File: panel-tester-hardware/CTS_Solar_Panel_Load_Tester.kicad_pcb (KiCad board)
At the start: 2 copper layers, 102 x 64.5 mm, 13 parts, among them J1 Screw_Terminal_01x02, J2 Conn_01x02_Pin, J3 Conn_01x07, J4 Conn_01x20_Pin, J5 Conn_01x20_Pin, Q2 2N7002, U1 INA219AxD, U3 LM311

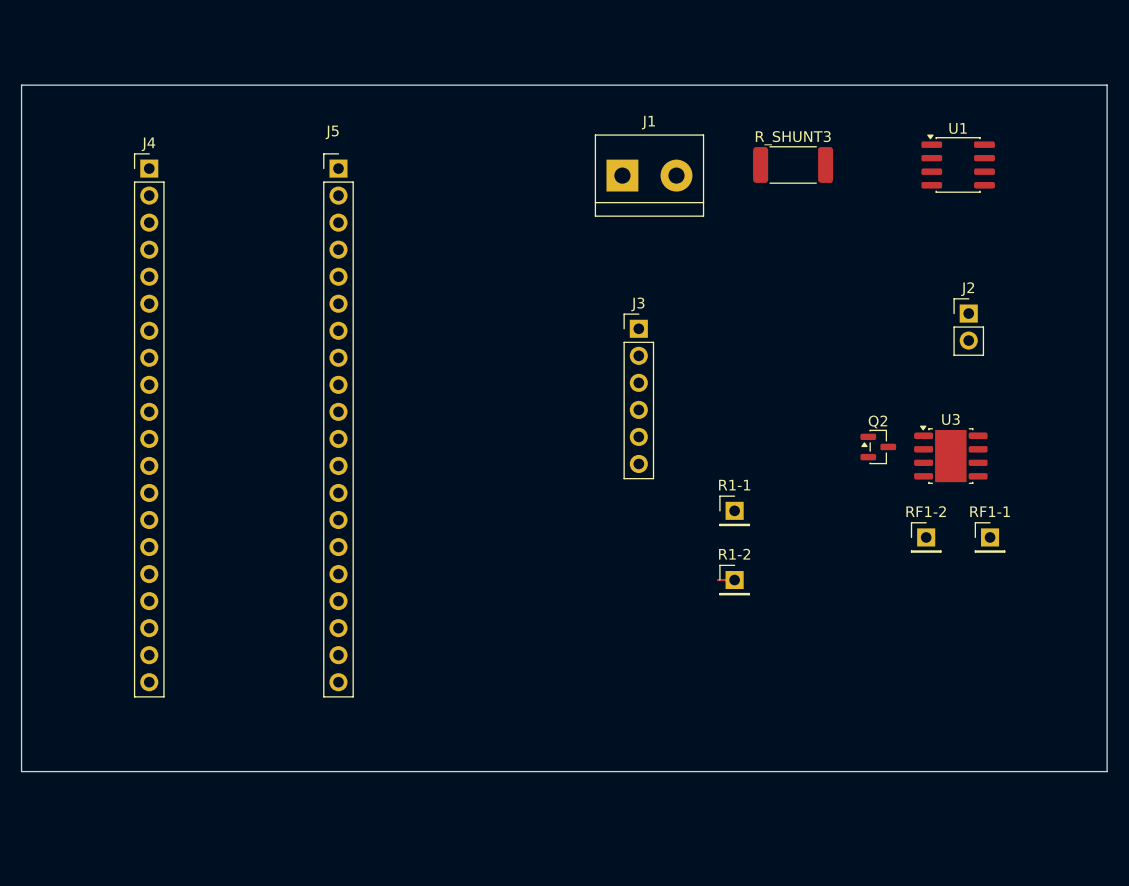
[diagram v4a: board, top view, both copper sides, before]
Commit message: PCB passes DRC
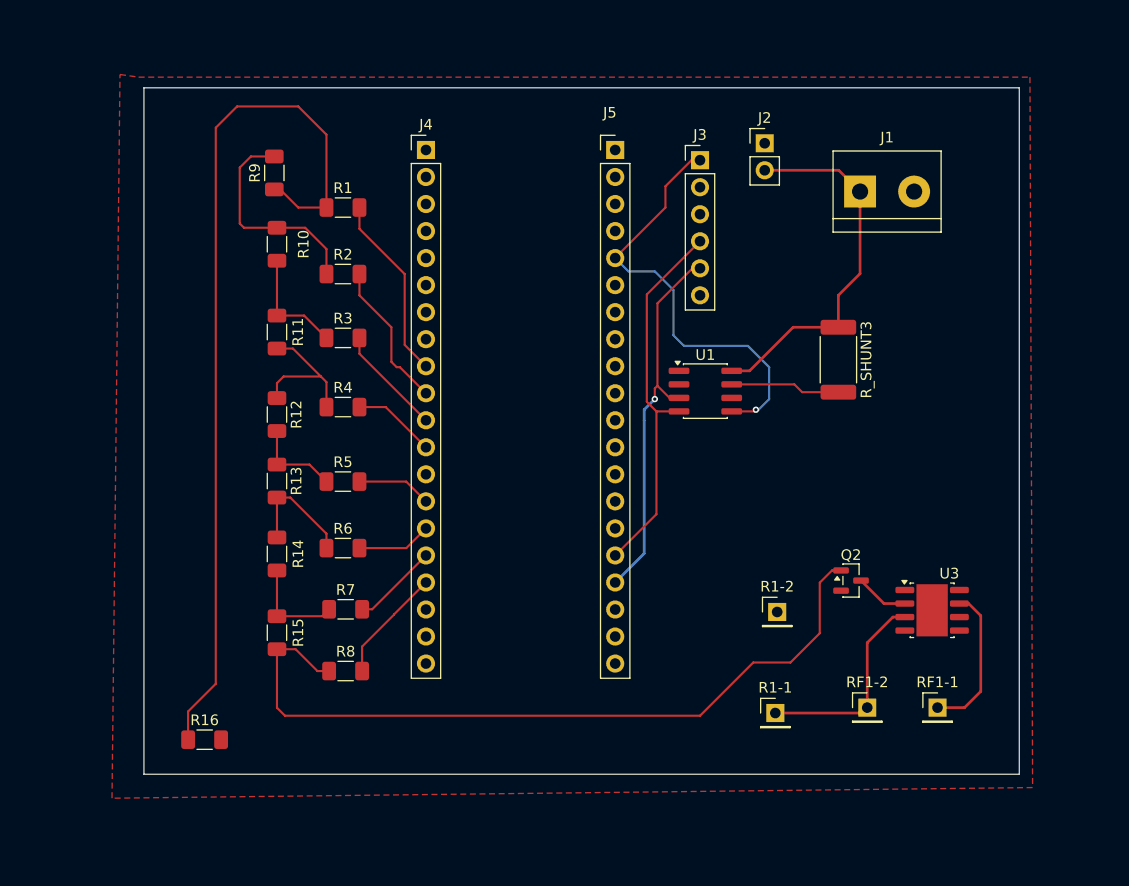
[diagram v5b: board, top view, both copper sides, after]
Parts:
- added R1: 2k, Resistor_SMD:R_1206_3216Metric_Pad1.30x1.75mm_HandSolder, F.Cu at (108.2, 65.0)
- added R10: 1k, Resistor_SMD:R_1206_3216Metric_Pad1.30x1.75mm_HandSolder, F.Cu at (102.0, 68.5)
- added R11: 1k, Resistor_SMD:R_1206_3216Metric_Pad1.30x1.75mm_HandSolder, F.Cu at (102.0, 76.7)
- added R12: 1k, Resistor_SMD:R_1206_3216Metric_Pad1.30x1.75mm_HandSolder, F.Cu at (102.0, 84.5)
- added R13: 1k, Resistor_SMD:R_1206_3216Metric_Pad1.30x1.75mm_HandSolder, F.Cu at (102.0, 90.7)
- added R14: 1k, Resistor_SMD:R_1206_3216Metric_Pad1.30x1.75mm_HandSolder, F.Cu at (102.0, 97.5)
- added R15: 1k, Resistor_SMD:R_1206_3216Metric_Pad1.30x1.75mm_HandSolder, F.Cu at (102.0, 105.0)
- added R16: 2k, Resistor_SMD:R_1206_3216Metric_Pad1.30x1.75mm_HandSolder, F.Cu at (95.2, 115.0)
- added R2: 2k, Resistor_SMD:R_1206_3216Metric_Pad1.30x1.75mm_HandSolder, F.Cu at (108.2, 71.2)
- added R3: 2k, Resistor_SMD:R_1206_3216Metric_Pad1.30x1.75mm_HandSolder, F.Cu at (108.2, 77.2)
- added R4: 2k, Resistor_SMD:R_1206_3216Metric_Pad1.30x1.75mm_HandSolder, F.Cu at (108.2, 83.8)
- added R5: 2k, Resistor_SMD:R_1206_3216Metric_Pad1.30x1.75mm_HandSolder, F.Cu at (108.2, 90.8)
- added R6: 2k, Resistor_SMD:R_1206_3216Metric_Pad1.30x1.75mm_HandSolder, F.Cu at (108.2, 97.0)
- added R7: 2k, Resistor_SMD:R_1206_3216Metric_Pad1.30x1.75mm_HandSolder, F.Cu at (108.5, 102.8)
- added R8: 2k, Resistor_SMD:R_1206_3216Metric_Pad1.30x1.75mm_HandSolder, F.Cu at (108.5, 108.6)
- added R9: 1k, Resistor_SMD:R_1206_3216Metric_Pad1.30x1.75mm_HandSolder, F.Cu at (101.8, 61.8)
- moved U1 31.9 mm to (142.2, 82.2)
- moved J4 26.1 mm to (116.0, 59.6)
- moved J5 26.1 mm to (133.8, 59.6)
- moved J2 25.0 mm to (147.8, 59.0)
- moved J1 22.4 mm to (156.8, 63.5)
- moved R1-1 19.4 mm to (148.8, 112.5)
- moved R_SHUNT3 18.8 mm to (154.8, 79.3), turned to -90 degrees
- moved RF1-2 16.9 mm to (157.5, 112.0)
- moved J3 16.9 mm to (141.8, 60.5)
- moved RF1-1 16.7 mm to (164.1, 112.0)
- moved U3 14.6 mm to (163.6, 102.8)
- moved Q2 12.8 mm to (155.9, 100.0)
- moved R1-2 5.00 mm to (149.0, 103.0)
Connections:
- J4 pad 10: unconnected-(J4-Pin_10-Pad10) -> GP7
- J4 pad 11: unconnected-(J4-Pin_11-Pad11) -> GP8
- J4 pad 12: unconnected-(J4-Pin_12-Pad12) -> GP9
- J4 pad 14: unconnected-(J4-Pin_14-Pad14) -> GP10
- J4 pad 15: unconnected-(J4-Pin_15-Pad15) -> GP11
- J4 pad 16: unconnected-(J4-Pin_16-Pad16) -> GP12
- J4 pad 17: unconnected-(J4-Pin_17-Pad17) -> GP13_MSB
- J4 pad 9: unconnected-(J4-Pin_9-Pad9) -> GP6_LSB
- J5 pad 16: unconnected-(J5-Pin_16-Pad16) -> MCU_I2C_SCL
- J5 pad 17: unconnected-(J5-Pin_17-Pad17) -> MCU_I2C_SDA
- J5 pad 18: unconnected-(J5-Pin_18-Pad18) -> GND
- J5 pad 5: unconnected-(J5-Pin_5-Pad5) -> +3V3
- Q2 pad 1: unconnected-(Q2-G-Pad1) -> RAMP
- U3 pad 1: Net-(U3-GND) -> GND
- U3 pad 4: Net-(U3-GND) -> GND
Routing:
- net Net-(R1-Pad1): track 0.00 -> 83.4 mm
- net RAMP: track 0.00 -> 73.0 mm
- net +3V3: track 0.00 -> 41.2 mm, vias 0 -> 1
- net MCU_I2C_SDA: track 0.00 -> 35.7 mm, vias 0 -> 1
- net MCU_I2C_SCL: track 0.00 -> 35.7 mm
- net V_SOLAR_INPUT_POS: track 0.00 -> 35.1 mm
- net Net-(R10-Pad1): track 0.00 -> 20.5 mm
- net Net-(R1-1-Pin_1): track 0.00 -> 19.5 mm
- net GP6_LSB: track 0.00 -> 17.5 mm
- net Net-(RF1-1-Pin_1): track 0.00 -> 14.3 mm
- net Net-(R11-Pad2): track 0.00 -> 14.1 mm
- net GP7: track 0.00 -> 14.0 mm
- net Net-(R13-Pad2): track 0.00 -> 11.2 mm
- net GP13_MSB: track 0.00 -> 10.8 mm
- net Net-(R10-Pad2): track 0.00 -> 10.7 mm
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- added copper zone on F.Cu, net GND
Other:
- board size 102 x 64.5 mm -> 82.2 x 64.5 mm

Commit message: checklist almost done
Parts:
- added G***: LOGO, 00-logo-footprint-library:ctslogo1x2cm, F.Cu at (147.2, 92.8)
- moved R16 56.8 mm to (108.2, 59.8)
- moved J1 7.96 mm to (154.2, 71.0), turned to 90 degrees
- moved Q2 4.36 mm to (151.6, 100.7)
- moved R1-1 4.36 mm to (144.5, 113.2)
- moved R1-2 4.36 mm to (144.7, 103.7)
- moved RF1-2 4.36 mm to (153.2, 112.6)
- moved U3 4.36 mm to (159.2, 103.5)
- moved RF1-1 4.36 mm to (159.8, 112.6)
- moved R_SHUNT3 4.04 mm to (151.5, 81.7)
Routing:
- net Net-(R1-Pad1): track 83.4 -> 10.9 mm
- net RAMP: track 73.0 -> 68.5 mm
- net Net-(U1-IN-): track 10.3 -> 8.07 mm
- net V_SOLAR_INPUT_POS: track 35.1 -> 33.6 mm
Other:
- board size 82.2 x 64.5 mm -> 70.2 x 64.5 mm
- board text added: "Solar Panel Load Tester rev3 2026-01-17"
